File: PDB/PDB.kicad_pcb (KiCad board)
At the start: 2 copper layers, 42 parts, among them Q1 S8050, Sw1 D-SWITCH_MR5-111-C5N-BB

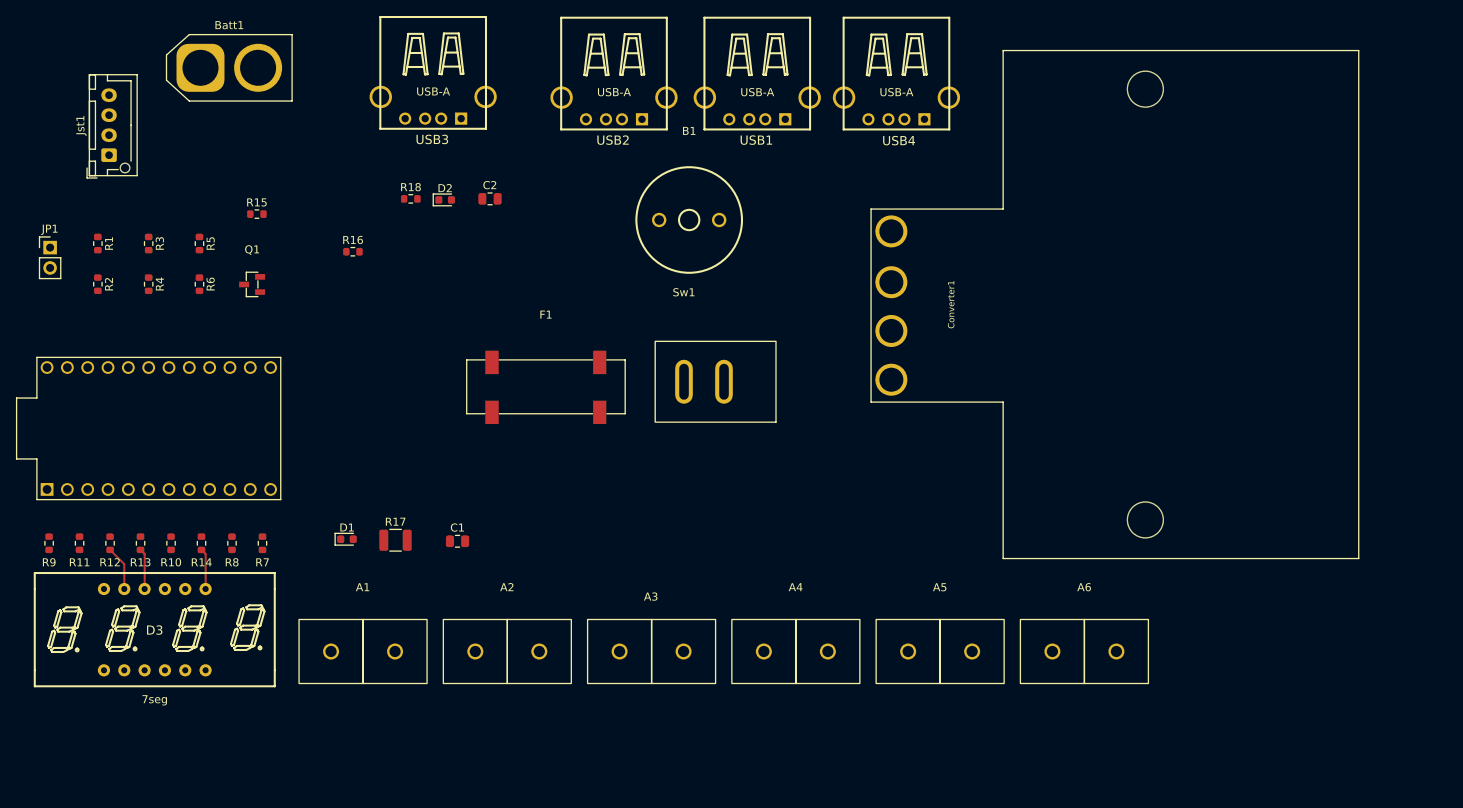
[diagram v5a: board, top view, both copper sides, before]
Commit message: Completed board layout
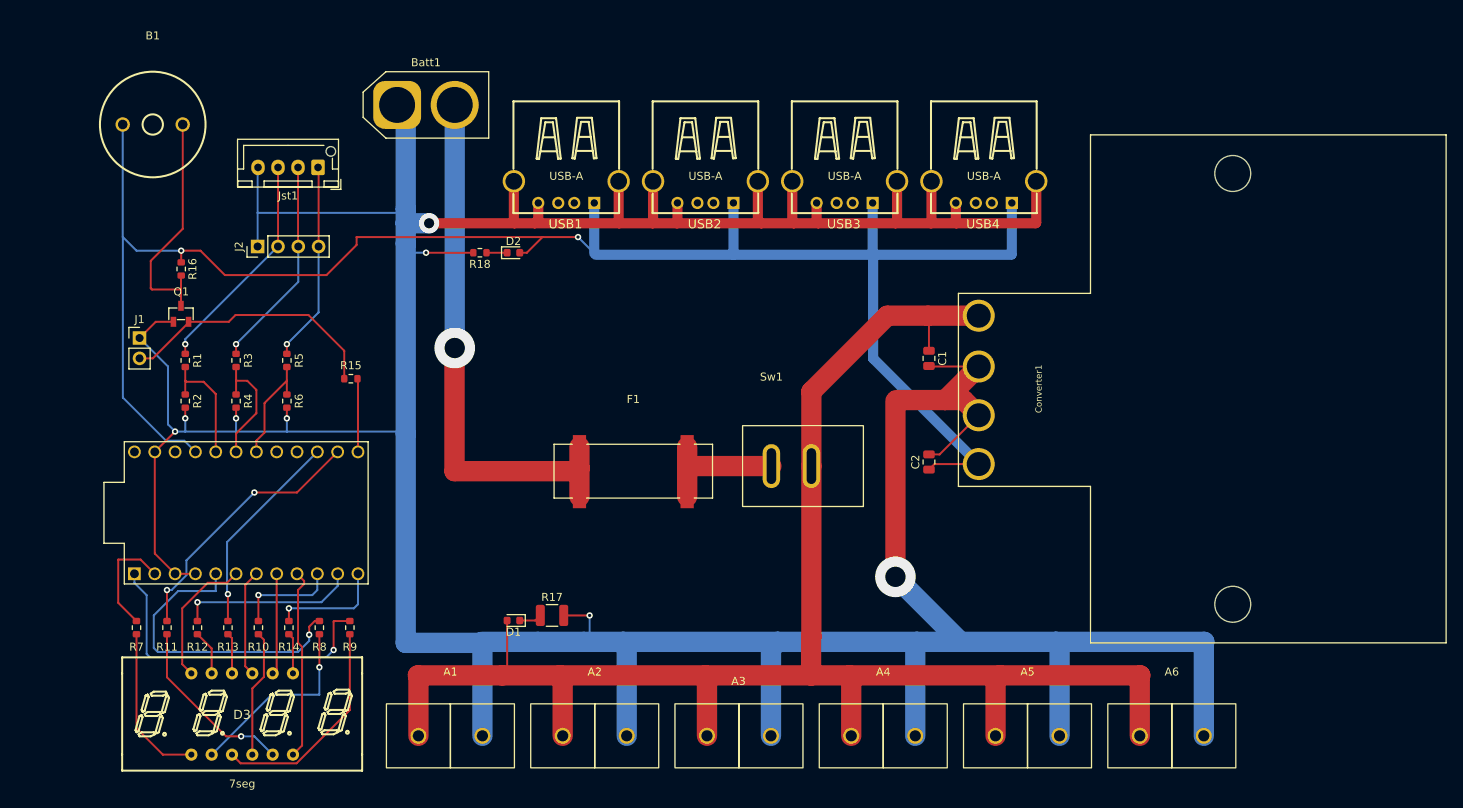
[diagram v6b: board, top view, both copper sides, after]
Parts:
- removed JP1: Jumper_2_Open, Connector_PinHeader_2.54mm:PinHeader_1x02_P2.54mm_Vertical
- added J1: Conn_01x02, Connector_PinHeader_2.54mm:PinHeader_1x02_P2.54mm_Vertical, F.Cu at (32.4, 59.4)
- added J2: Conn_01x04, Connector_PinHeader_2.54mm:PinHeader_1x04_P2.54mm_Vertical, F.Cu at (47.1, 48.0)
- moved B1 68.1 mm to (34.0, 32.6)
- moved C2 64.0 mm to (131.1, 74.9), turned to 90 degrees
- moved C1 63.2 mm to (131.1, 62.0), turned to -90 degrees
- moved USB3 52.5 mm to (120.5, 41.2)
- moved R9 39.0 mm to (58.7, 95.6)
- moved Jst1 26.2 mm to (54.7, 38.1), turned to 180 degrees
- moved USB1 26.1 mm to (85.7, 41.2)
- moved Batt1 25.0 mm to (64.6, 30.3)
- moved R15 23.7 mm to (58.8, 64.5), turned to 180 degrees
- moved D1 23.2 mm to (79.1, 94.7), turned to 180 degrees
- moved R17 21.7 mm to (83.9, 94.1)
- moved R16 21.6 mm to (37.6, 50.8), turned to -90 degrees
- moved R7 19.0 mm to (32.0, 95.6)
- moved R4 18.2 mm to (44.5, 67.3), turned to 90 degrees
- moved R1 18.2 mm to (38.1, 62.2)
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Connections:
- Pro1 pad 18: /Cell1_s -> /Cell1+2+3_s
- Pro1 pad 20: /Cell1+2+3_s -> /Cell1_s
- Pro1 pad 6: /Dig4 -> /Dig1
- Pro1 pad 7: /Dig3 -> /Dig2
- Pro1 pad 8: /Dig2 -> /Dig3
- Pro1 pad 9: /Dig1 -> /Dig4
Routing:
- net GND: track 0.00 -> 556.4 mm, vias 0 -> 8
- net /5v: track 0.00 -> 231.5 mm, vias 0 -> 2
- net /12v: track 0.00 -> 208.1 mm
- net /battery: track 0.00 -> 67.8 mm, vias 0 -> 1
- net /DP: track 0.00 -> 40.2 mm, vias 0 -> 1
- net /D: track 0.00 -> 38.8 mm, vias 0 -> 1
- net /G: track 0.00 -> 33.4 mm, vias 0 -> 2
- net Net-(J1-Pad2): track 0.00 -> 33.2 mm
- net Net-(B1-Pad2): track 0.00 -> 29.8 mm
- net /Cell1: track 0.00 -> 28.1 mm, vias 0 -> 1
- net Net-(D3-Pad3): track 0.00 -> 27.4 mm
- net /Cell1+2: track 0.00 -> 26.5 mm, vias 0 -> 1
- net /F: track 0.00 -> 25.9 mm, vias 0 -> 1
- net /Cell1+2+3: track 0.00 -> 25.0 mm, vias 0 -> 1
- net Net-(D3-Pad2): track 0.00 -> 24.1 mm, vias 0 -> 1
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
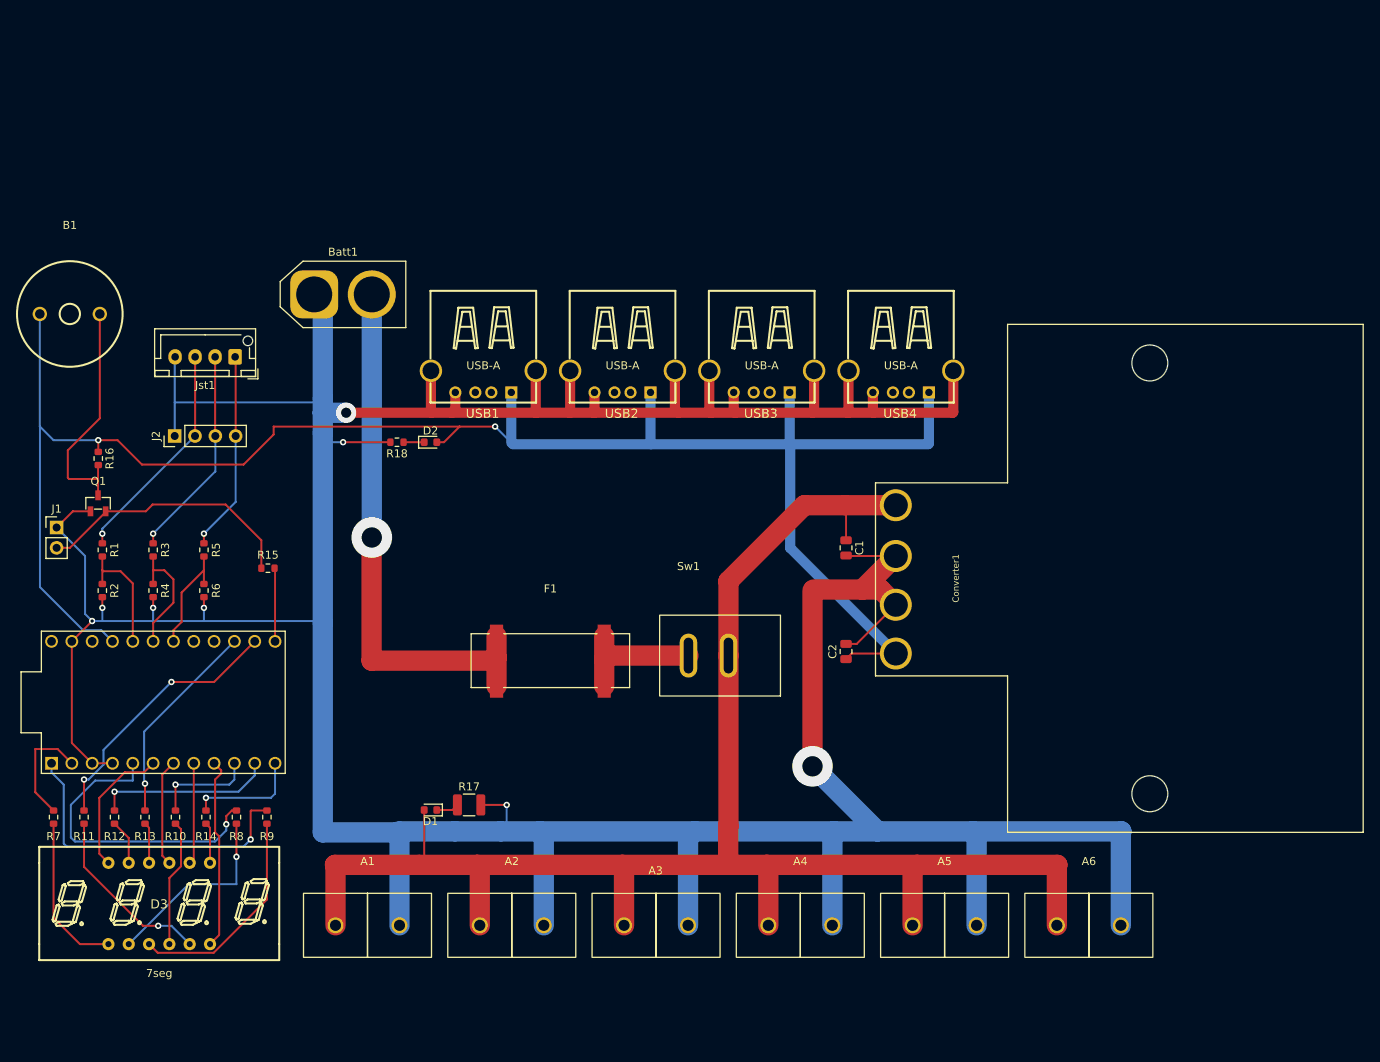
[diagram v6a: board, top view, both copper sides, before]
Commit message: revised layout for smaller size
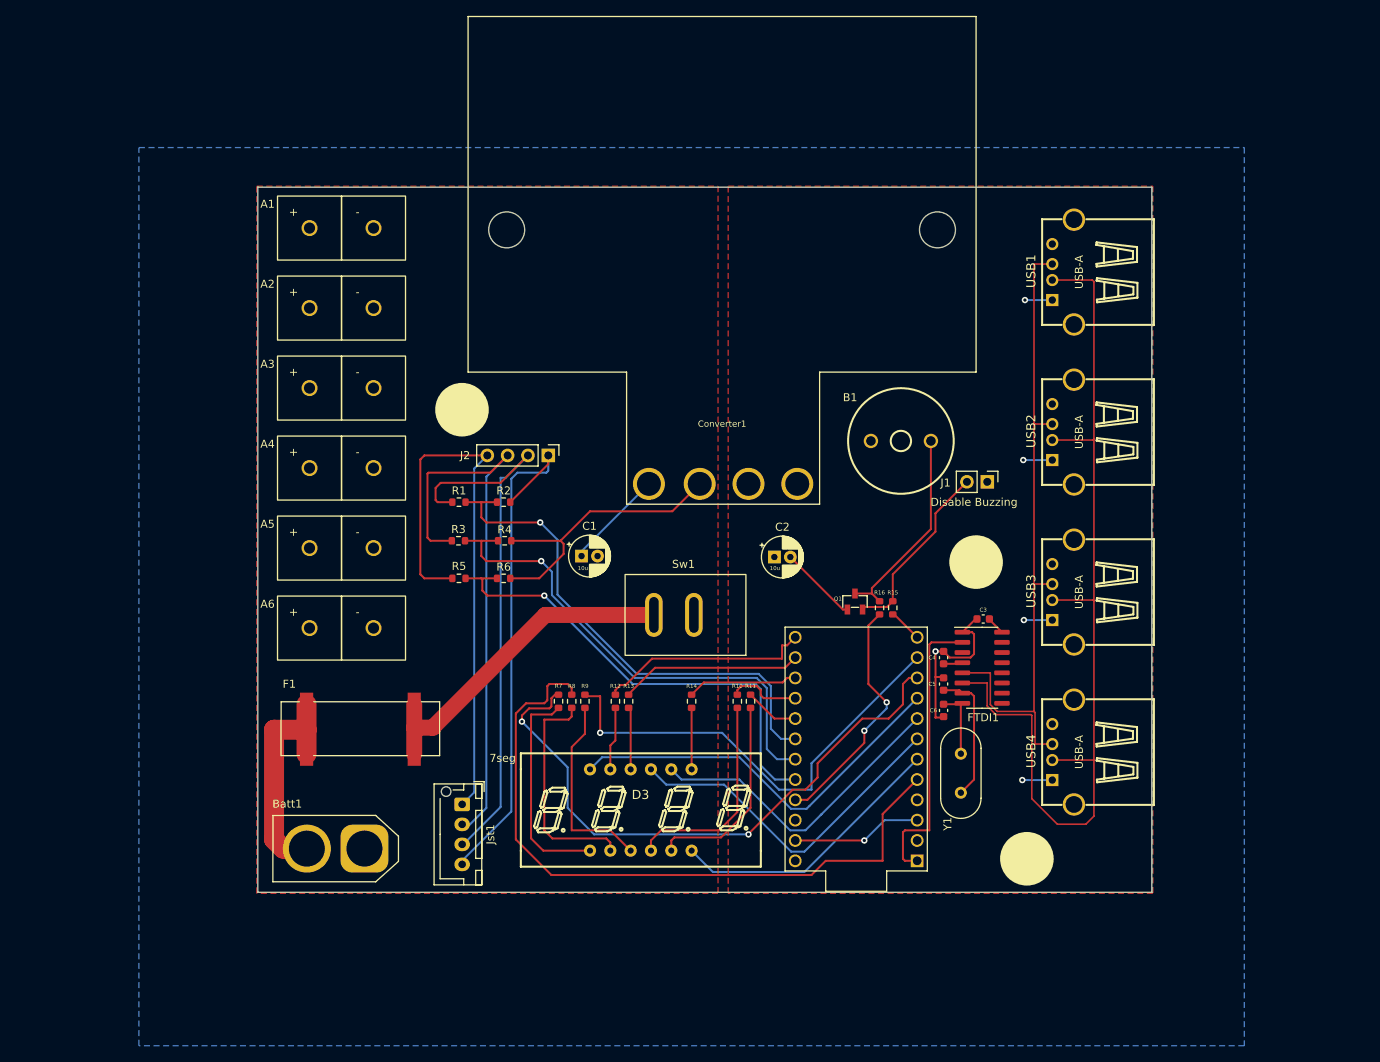
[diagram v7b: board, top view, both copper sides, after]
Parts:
- removed D1, D2: LED, LED_SMD:LED_0603_1608Metric
- removed R17: 590, Resistor_SMD:R_1210_3225Metric
- removed R18: 120, Resistor_SMD:R_0603_1608Metric
- added C3: 0.1uF, Capacitor_SMD:C_0603_1608Metric, F.Cu at (148.2, 70.9)
- added C4: 0.1uF, Capacitor_SMD:C_0603_1608Metric, F.Cu at (143.3, 75.7)
- added C5: 22pF, Capacitor_SMD:C_0603_1608Metric, F.Cu at (143.3, 79.0)
- added C6: 22pF, Capacitor_SMD:C_0603_1608Metric, F.Cu at (143.3, 82.3)
- added FTDI1: CH340G, Package_SO:SOIC-16_3.9x9.9mm_P1.27mm, F.Cu at (148.1, 77.0)
- added Y1: 12MHz, Crystal:Crystal_HC49-U_Vertical, F.Cu at (145.4, 92.6)
- C1, C2: footprint Capacitor_SMD:C_0805_2012Metric -> Capacitor_THT:CP_Radial_D5.0mm_P2.00mm
- moved J1 116.5 mm to (148.7, 53.7), turned to -90 degrees
- moved B1 105.1 mm to (137.9, 48.5)
- moved A6 100.5 mm to (68.0, 68.0)
- moved R16 99.4 mm to (135.3, 69.5), turned to 90 degrees
- moved Q1 95.4 mm to (132.2, 68.7)
- moved A5 88.9 mm to (68.0, 58.0)
- moved A1 87.2 mm to (68.0, 18.0)
- moved Pro1 86.8 mm to (132.3, 87.1), turned to 90 degrees
- moved R11 84.6 mm to (119.1, 81.2)
- moved A4 81.0 mm to (68.0, 48.0)
- moved A2 80.0 mm to (68.0, 28.0)
- moved R15 78.3 mm to (136.9, 69.5), turned to 90 degrees
- moved A3 77.8 mm to (68.0, 38.0)
- moved USB1 73.8 mm to (158.2, 27.5), turned to 90 degrees
- moved R10 71.7 mm to (117.5, 81.2)
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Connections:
- Pro1 pad 1: /DP -> /Tx
- Pro1 pad 10: /C -> /E
- Pro1 pad 11: /A -> /DP
- Pro1 pad 12: /B -> /Buzzer
- Pro1 pad 13: /Buzzer -> /A
- Pro1 pad 14: /G -> /F
- Pro1 pad 15: /F -> /B
- Pro1 pad 16: unconnected-(Pro1-Pad16) -> /C
- Pro1 pad 17: unconnected-(Pro1-Pad17) -> /G
- Pro1 pad 18: /Cell1+2+3_s -> /Cell1_s
- Pro1 pad 2: /E -> /toggle
- Pro1 pad 20: /Cell1_s -> /Cell1+2+3_s
- Pro1 pad 6: /Dig1 -> /Dig4
- Pro1 pad 9: /Dig4 -> /Dig1
- USB1 pad 2: unconnected-(USB1-Pad2) -> /D-
- USB1 pad 3: unconnected-(USB1-Pad3) -> /D+
- USB2 pad 2: unconnected-(USB2-Pad2) -> /D-
- USB2 pad 3: unconnected-(USB2-Pad3) -> /D+
- USB3 pad 2: unconnected-(USB3-Pad2) -> /D-
- USB3 pad 3: unconnected-(USB3-Pad3) -> /D+
- USB4 pad 2: unconnected-(USB4-Pad2) -> /D-
- USB4 pad 3: unconnected-(USB4-Pad3) -> /D+
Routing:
- net GND: track 556.4 -> 150.0 mm, vias 8 -> 2
- net /12v: track 208.1 -> 12.5 mm
- net /5v: track 231.5 -> 47.0 mm, vias 2 -> 6
- net /D-: track 0.00 -> 119.8 mm
- net /D+: track 0.00 -> 82.4 mm
- net /E: track 13.9 -> 75.9 mm, vias 0 -> 2
- net /Cell1_s: track 15.2 -> 63.7 mm, vias 0 -> 1
- net /D: track 38.8 -> 86.7 mm, vias 1 -> 0
- net /Cell1+2+3: track 25.0 -> 72.1 mm, vias 1 -> 0
- net /Cell1+2_s: track 15.2 -> 62.0 mm, vias 0 -> 1
- net /Cell1+2+3_s: track 13.9 -> 60.0 mm, vias 0 -> 1
- net /Cell1+2: track 26.5 -> 71.2 mm, vias 1 -> 0
- net /Cell1: track 28.1 -> 69.4 mm, vias 1 -> 0
- net /battery: track 67.8 -> 28.6 mm, vias 1 -> 0
- net /Tx: track 0.00 -> 36.1 mm
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- added copper zone on F.Cu, net /12v
- added copper zone on F.Cu, net /5v
- added copper zone on B.Cu, net GND
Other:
- board outline added: 111.8 x 88.1 mm
- board text added: "10u"
- board text added: "Disable Buzzing"

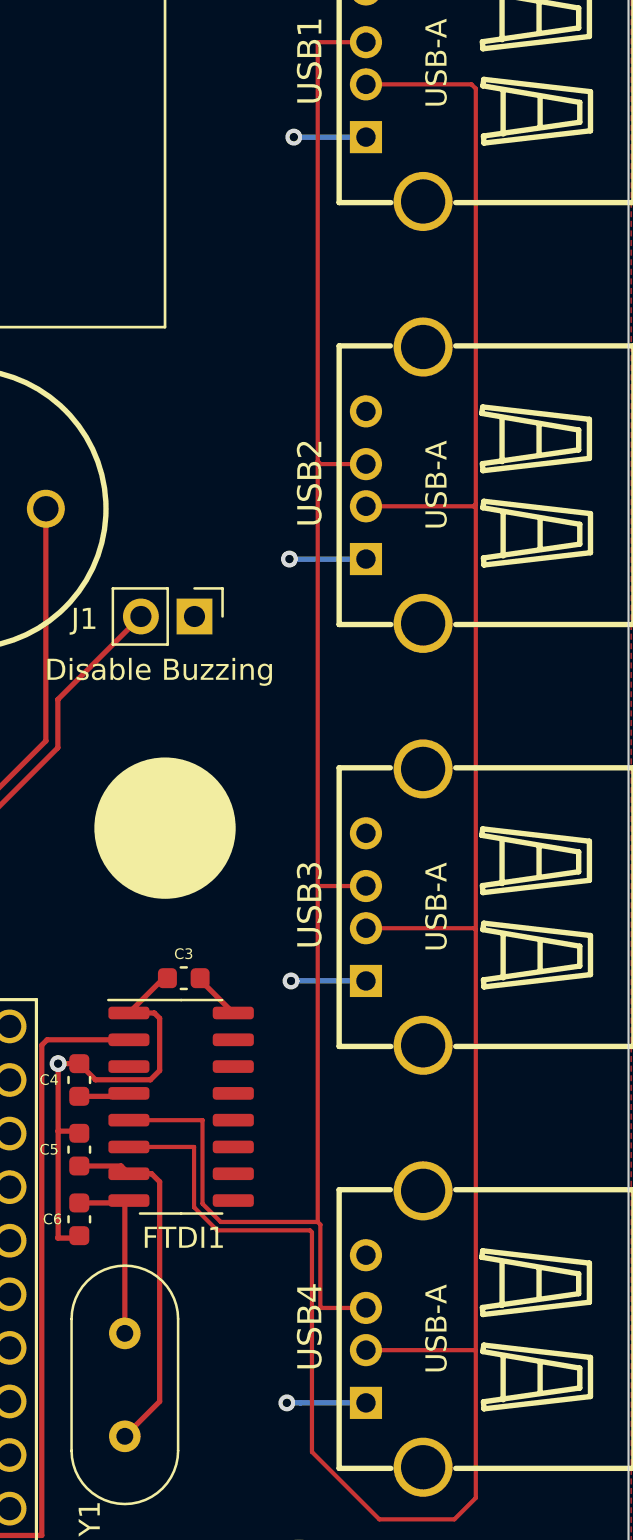
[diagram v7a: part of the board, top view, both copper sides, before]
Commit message: Increased track size for USB
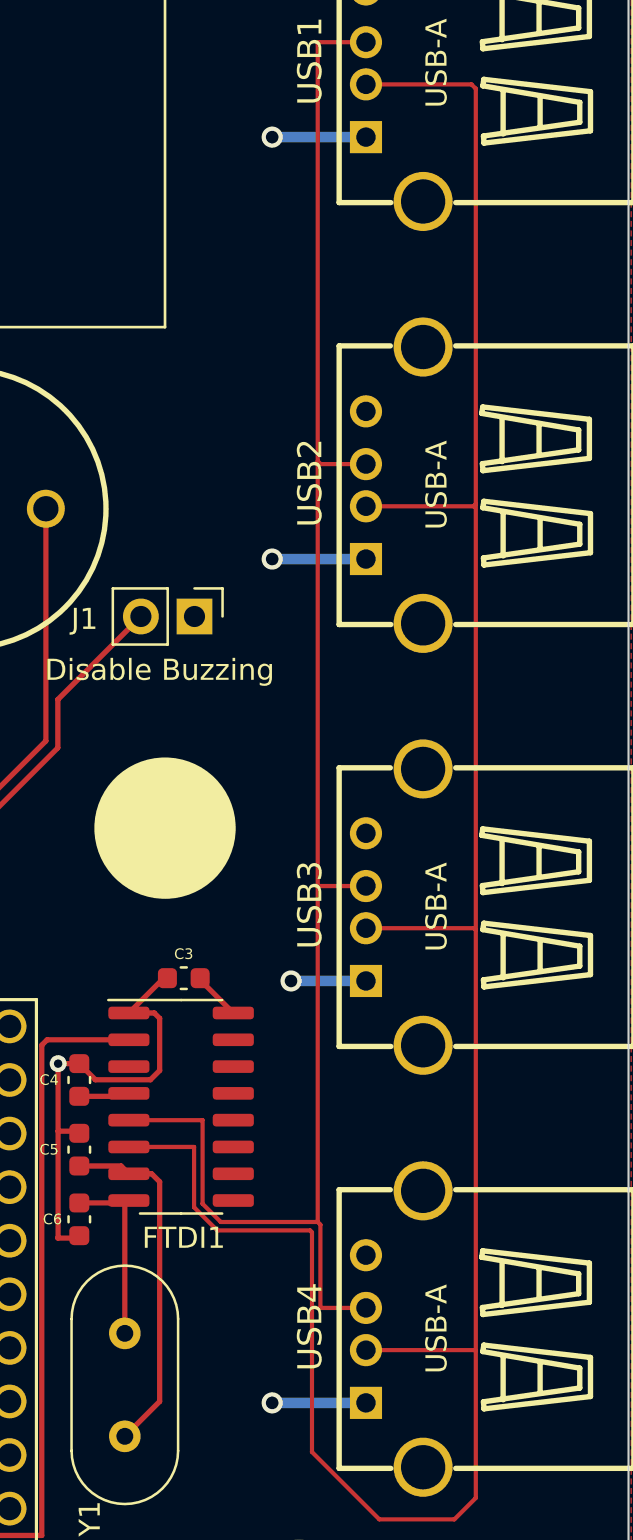
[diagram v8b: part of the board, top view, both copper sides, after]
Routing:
- net /5v: track 47.0 -> 49.5 mm
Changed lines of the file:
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@@
   (segment (start 148.984 70.866) (end 148.984 70.944) (width 0.25) (layer "F.Cu") (net 3))
   (segment (start 148.984 70.944) (end 150.557 72.517) (width 0.25) (layer "F.Cu") (net 3))
-  (via (at 153.218 50.998) (size 0.8) (drill 0.4) (layers "F.Cu" "B.Cu") (net 3))
+  (via (at 152.4 50.998) (size 1) (drill 0.6) (layers "F.Cu" "B.Cu") (net 3))
   (via (at 136.144 81.28) (size 0.8) (drill 0.4) (layers "F.Cu" "B.Cu") (net 3))
-  (via (at 153.096 90.998) (size 0.8) (drill 0.4) (layers "F.Cu" "B.Cu") (net 3))
-  (via (at 153.294 70.998) (size 0.8) (drill 0.4) (layers "F.Cu" "B.Cu") (net 3))
-  (via (at 153.426 30.998) (size 0.8) (drill 0.4) (layers "F.Cu" "B.Cu") (net 3))
+  (via (at 152.4 90.998) (size 1) (drill 0.6) (layers "F.Cu" "B.Cu") (net 3))
+  (via (at 153.294 70.998) (size 1) (drill 0.6) (layers "F.Cu" "B.Cu") (net 3))
+  (via (at 152.4 30.998) (size 1) (drill 0.6) (layers "F.Cu" "B.Cu") (net 3))
   (via (at 133.35 84.836) (size 0.8) (drill 0.4) (layers "F.Cu" "B.Cu") (net 3))
-  (segment (start 156.845 70.998) (end 153.294 70.998) (width 0.25) (layer "B.Cu") (net 3))
-  (segment (start 153.426 30.998) (end 156.845 30.998) (width 0.25) (layer "B.Cu") (net 3))
-  (segment (start 153.736 90.998) (end 153.096 90.998) (width 0.25) (layer "B.Cu") (net 3))
-  (segment (start 153.218 50.998) (end 156.845 50.998) (width 0.25) (layer "B.Cu") (net 3))
+  (segment (start 156.845 70.998) (end 153.294 70.998) (width 0.5) (layer "B.Cu") (net 3))
+  (segment (start 152.4 50.998) (end 156.845 50.998) (width 0.5) (layer "B.Cu") (net 3))
   (segment (start 133.35 84.836) (end 136.144 82.042) (width 0.25) (layer "B.Cu") (net 3))
   (segment (start 136.144 82.042) (end 136.144 81.28) (width 0.25) (layer "B.Cu") (net 3))
-  (segment (start 153.736 90.998) (end 156.845 90.998) (width 0.25) (layer "B.Cu") (net 3))
+  (segment (start 152.4 90.998) (end 156.845 90.998) (width 0.5) (layer "B.Cu") (net 3))
+  (segment (start 152.4 30.998) (end 156.845 30.998) (width 0.5) (layer "B.Cu") (net 3))
   (segment (start 134.294 67.001) (end 141.672 59.623) (width 0.25) (layer "F.Cu") (net 4))
   (segment (start 134.294 67.683) (end 134.294 67.001) (width 0.25) (layer "F.Cu") (net 4))
